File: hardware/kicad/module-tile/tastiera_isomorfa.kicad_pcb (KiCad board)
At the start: 2 copper layers, 87 x 97.2 mm, 67 parts, among them J101 Conn_LEFT, J102 Conn_TOP, J103 Conn_BOTTOM, J104 Conn_RIGHT, J105 BTNs_L_MSB, J106 BTNs_L_LSB, J107 BTNs_MSB, J108 BTNs_LSB, SW101 SW_Push, SW102 SW_Push, SW103 SW_Push, SW104 SW_Push, SW105 SW_Push, SW106 SW_Push, SW107 SW_Push, SW108 SW_Push, SW109 SW_Push, SW110 SW_Push, SW111 SW_Push, SW112 SW_Push, U101 74AUC2G126, U102 74AUC2G08, U103 74HC165, U104 74HC165, U105 74AHC1G04, U106 74LVC2G32, U107 74AUC2G125, U108 74LVC2G74, U109 74LS161

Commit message: Create gerber files
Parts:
- added REF**10: Senza-titolo, Senza-titolo, F.Cu at (124.5, 95.8)
- added REF**10: Senza-titolo, Senza-titolo, F.Cu at (166.5, 109.0)
- added REF**10: Senza-titolo, Senza-titolo, F.Cu at (124.6, 109.0)
- added REF**10: Senza-titolo, Senza-titolo, F.Cu at (165.5, 95.8)
- added REF**11: Senza-titolo, Senza-titolo, F.Cu at (125.3, 95.8)
- added REF**11: Senza-titolo, Senza-titolo, F.Cu at (166.3, 95.8)
- added REF**11: Senza-titolo, Senza-titolo, F.Cu at (167.3, 109.0)
- added REF**11: Senza-titolo, Senza-titolo, F.Cu at (125.4, 109.0)
- added REF**12: Senza-titolo, Senza-titolo, F.Cu at (126.1, 95.8)
- added REF**12: Senza-titolo, Senza-titolo, F.Cu at (126.2, 109.0)
- added REF**12: Senza-titolo, Senza-titolo, F.Cu at (168.1, 109.0)
- added REF**12: Senza-titolo, Senza-titolo, F.Cu at (167.1, 95.8)
- added REF**13: Senza-titolo, Senza-titolo, F.Cu at (167.9, 95.8)
- added REF**13: Senza-titolo, Senza-titolo, F.Cu at (168.9, 109.0)
- added REF**13: Senza-titolo, Senza-titolo, F.Cu at (127.0, 109.0)
- added REF**13: Senza-titolo, Senza-titolo, F.Cu at (126.9, 95.8)
- added REF**14: Senza-titolo, Senza-titolo, F.Cu at (127.7, 95.8)
- added REF**14: Senza-titolo, Senza-titolo, F.Cu at (169.7, 109.0)
- added REF**14: Senza-titolo, Senza-titolo, F.Cu at (127.8, 109.0)
- added REF**14: Senza-titolo, Senza-titolo, F.Cu at (168.7, 95.8)
- added REF**15: Senza-titolo, Senza-titolo, F.Cu at (169.5, 95.8)
- added REF**15: Senza-titolo, Senza-titolo, F.Cu at (128.5, 95.8)
- added REF**15: Senza-titolo, Senza-titolo, F.Cu at (170.5, 109.0)
- added REF**15: Senza-titolo, Senza-titolo, F.Cu at (128.6, 109.0)
- added REF**16: Senza-titolo, Senza-titolo, F.Cu at (170.3, 95.8)
- added REF**16: Senza-titolo, Senza-titolo, F.Cu at (129.3, 95.8)
- added REF**16: Senza-titolo, Senza-titolo, F.Cu at (171.3, 109.0)
- added REF**16: Senza-titolo, Senza-titolo, F.Cu at (129.4, 109.0)
- added REF**17: Senza-titolo, Senza-titolo, F.Cu at (172.1, 109.0)
- added REF**17: Senza-titolo, Senza-titolo, F.Cu at (171.1, 95.8)
- added REF**17: Senza-titolo, Senza-titolo, F.Cu at (130.2, 109.0)
- added REF**17: Senza-titolo, Senza-titolo, F.Cu at (130.1, 95.8)
- added REF**18: Senza-titolo, Senza-titolo, F.Cu at (172.9, 109.0)
- added REF**18: Senza-titolo, Senza-titolo, F.Cu at (131.0, 109.0)
- added REF**18: Senza-titolo, Senza-titolo, F.Cu at (171.9, 95.8)
- added REF**18: Senza-titolo, Senza-titolo, F.Cu at (130.9, 95.8)
- added REF**19: Senza-titolo, Senza-titolo, F.Cu at (131.8, 109.0)
- added REF**19: Senza-titolo, Senza-titolo, F.Cu at (172.7, 95.8)
- added REF**19: Senza-titolo, Senza-titolo, F.Cu at (131.7, 95.8)
- added REF**2: Senza-titolo, Senza-titolo, F.Cu at (160.1, 109.0)
- added REF**3: Senza-titolo, Senza-titolo, F.Cu at (159.9, 95.8)
- added REF**3: Senza-titolo, Senza-titolo, F.Cu at (118.9, 95.8)
- added REF**3: Senza-titolo, Senza-titolo, F.Cu at (119.0, 109.0)
- added REF**3: Senza-titolo, Senza-titolo, F.Cu at (160.9, 109.0)
- added REF**4: Senza-titolo, Senza-titolo, F.Cu at (119.7, 95.8)
- added REF**4: Senza-titolo, Senza-titolo, F.Cu at (119.8, 109.0)
- added REF**4: Senza-titolo, Senza-titolo, F.Cu at (160.7, 95.8)
- added REF**4: Senza-titolo, Senza-titolo, F.Cu at (161.7, 109.0)
- added REF**5: Senza-titolo, Senza-titolo, F.Cu at (162.5, 109.0)
- added REF**5: Senza-titolo, Senza-titolo, F.Cu at (120.6, 109.0)
- added REF**5: Senza-titolo, Senza-titolo, F.Cu at (120.5, 95.8)
- added REF**5: Senza-titolo, Senza-titolo, F.Cu at (161.5, 95.8)
- added REF**6: Senza-titolo, Senza-titolo, F.Cu at (121.3, 95.8)
- added REF**6: Senza-titolo, Senza-titolo, F.Cu at (121.4, 109.0)
- added REF**6: Senza-titolo, Senza-titolo, F.Cu at (162.3, 95.8)
- added REF**6: Senza-titolo, Senza-titolo, F.Cu at (163.3, 109.0)
- added REF**7: Senza-titolo, Senza-titolo, F.Cu at (122.1, 95.8)
- added REF**7: Senza-titolo, Senza-titolo, F.Cu at (122.2, 109.0)
- added REF**7: Senza-titolo, Senza-titolo, F.Cu at (164.1, 109.0)
- added REF**7: Senza-titolo, Senza-titolo, F.Cu at (163.1, 95.8)
- added REF**8: Senza-titolo, Senza-titolo, F.Cu at (163.9, 95.8)
- added REF**8: Senza-titolo, Senza-titolo, F.Cu at (123.0, 109.0)
- added REF**8: Senza-titolo, Senza-titolo, F.Cu at (164.9, 109.0)
- added REF**8: Senza-titolo, Senza-titolo, F.Cu at (122.9, 95.8)
- added REF**9: Senza-titolo, Senza-titolo, F.Cu at (123.7, 95.8)
- added REF**9: Senza-titolo, Senza-titolo, F.Cu at (164.7, 95.8)
- added REF**9: Senza-titolo, Senza-titolo, F.Cu at (165.7, 109.0)
- added REF**9: Senza-titolo, Senza-titolo, F.Cu at (123.8, 109.0)
- moved C104 45.2 mm to (124.8, 115.0)
- moved SW102 24.1 mm to (138.5, 48.0)
- moved R110 24.1 mm to (153.0, 57.5)
- moved R111 24.1 mm to (133.0, 57.5)
- moved R116 24.1 mm to (193.0, 57.5)
- moved R117 24.1 mm to (173.0, 57.5)
- moved R122 24.1 mm to (146.0, 50.5)
- moved R123 24.1 mm to (146.0, 56.0)
- moved R128 24.1 mm to (186.0, 56.0)
- moved R129 24.1 mm to (186.0, 50.5)
- moved SW101 24.1 mm to (158.5, 48.0)
- moved SW107 24.1 mm to (198.5, 48.0)
- moved SW108 24.1 mm to (178.5, 48.0)
- moved J102 20.9 mm to (159.0, 112.5)
- moved J103 20.8 mm to (149.0, 150.2)
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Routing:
- net GND: track 406.1 -> 215.2 mm
- net VCC_T: track 113.7 -> 39.3 mm
- net VCC: track 261.8 -> 209.1 mm
- net GND_T: track 49.3 -> 24.7 mm
- net /keyboard/BTNs1: track 25.7 -> 9.71 mm
- net /keyboard/BTNs7: track 25.7 -> 9.79 mm
- net /keyboard/BTNs0: track 7.17 -> 20.6 mm
- net /keyboard/BTNs6: track 7.25 -> 20.7 mm
- net /tile/T_data: track 10.5 -> 13.5 mm
- net /tile/B_first: track 33.1 -> 36.0 mm
- net /tile/B_latch: track 12.8 -> 15.3 mm
- net Net-(U109-Tc): track 33.1 -> 35.4 mm
- net /tile/T_W: track 16.1 -> 14.1 mm
- net /tile/B_clk: track 138.8 -> 140.7 mm
- net /tile/L_latch: track 83.9 -> 82.4 mm
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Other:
- board size 87 x 97.2 mm -> 97 x 109 mm

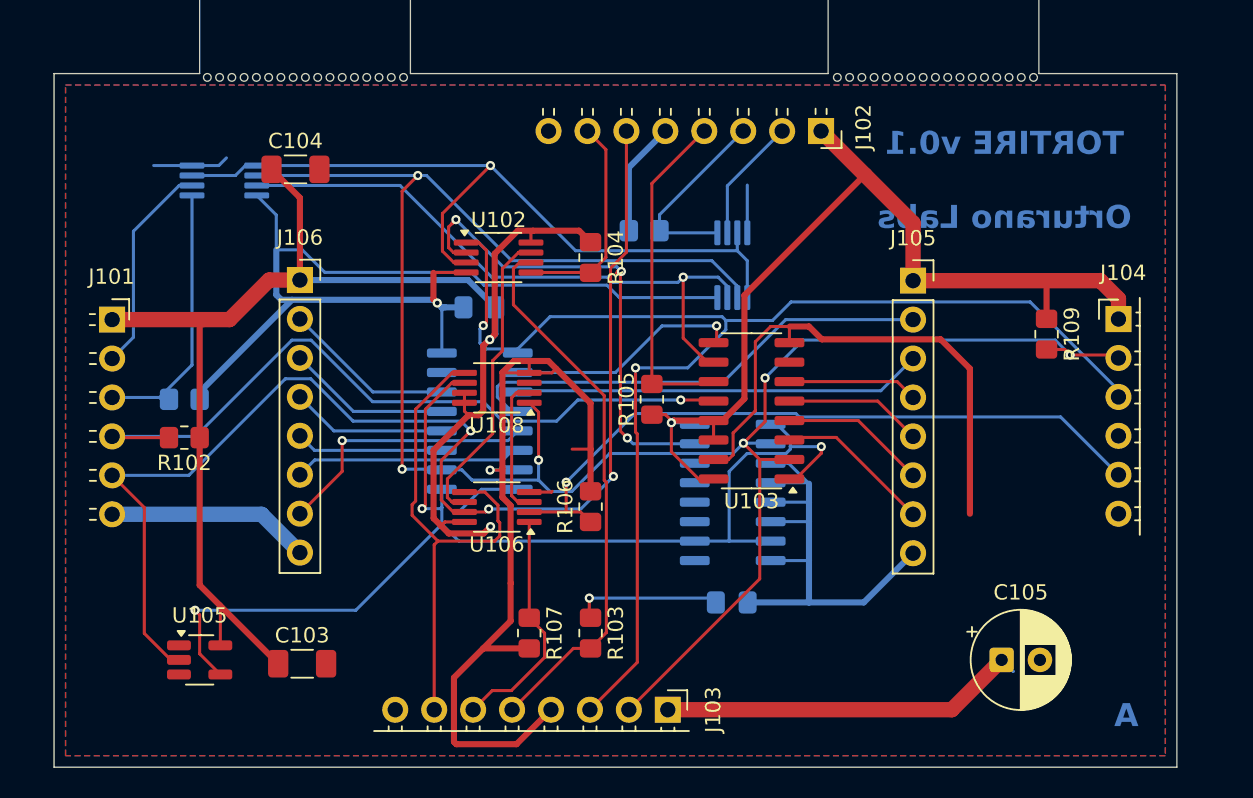
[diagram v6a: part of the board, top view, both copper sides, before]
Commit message: Adjust interboard pitch
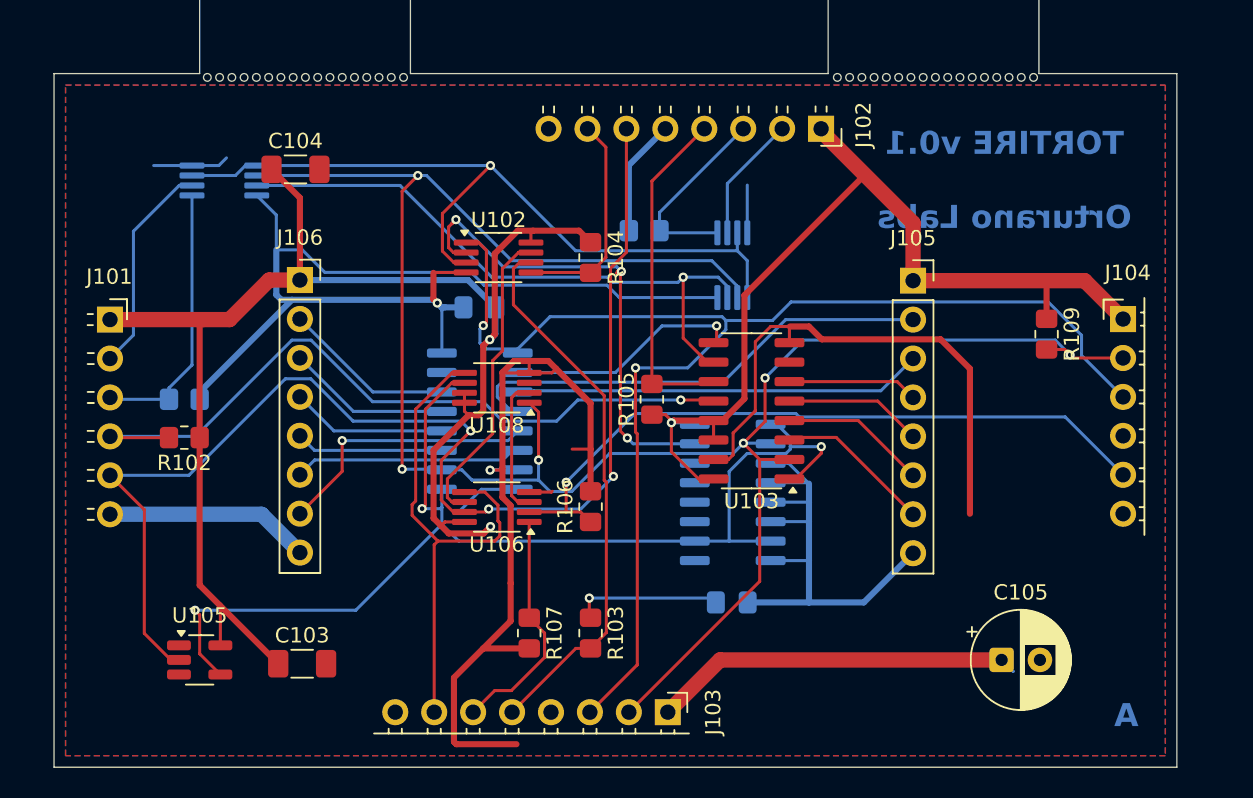
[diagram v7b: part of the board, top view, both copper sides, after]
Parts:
- moved J104 0.30 mm to (178.7, 124.8)
- moved J103 0.16 mm to (149.0, 150.4)
- moved J102 0.15 mm to (159.0, 112.3)
- moved J101 0.14 mm to (112.7, 124.8)
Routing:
- net GND: track 215.2 -> 212.3 mm
- net /tile/B_data: track 85.3 -> 86.7 mm
- net /tile/B_clk: track 140.7 -> 141.4 mm
